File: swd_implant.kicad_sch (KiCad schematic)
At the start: 24 parts, among them J1 U262-161N-4BVC11, J2 G&W pressure contact, J3 50 mil Pin Header, J4 SOICbite, J5 100 mil Pin Header, J6 100 mil Pin header, U1 ATSAMD21E18A, U2 AP2127K-3.3

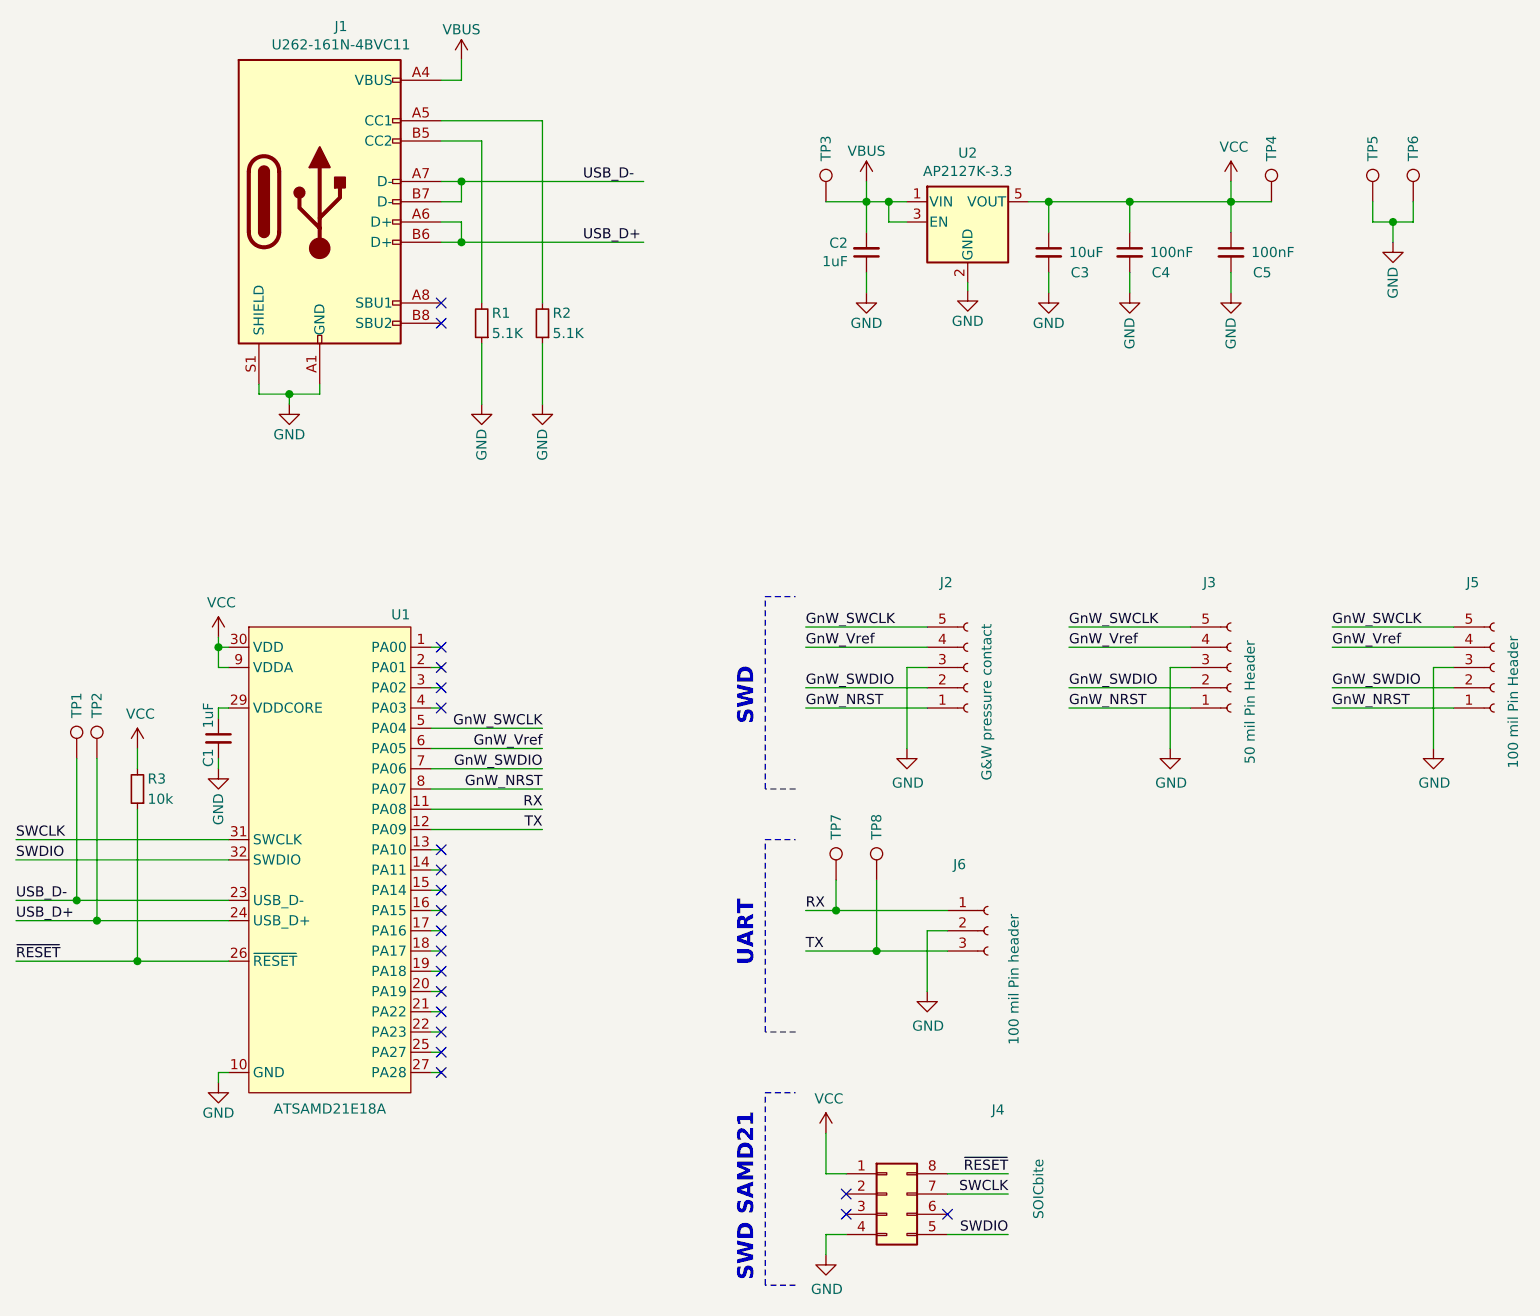
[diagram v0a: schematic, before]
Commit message: New board outline & swd pinout fixes
Changed the board outline to work with castellated edges, making it possible to
solder down instead of just relying on pressure contact.

Also fixed the inverted SWD pinout from upstream.
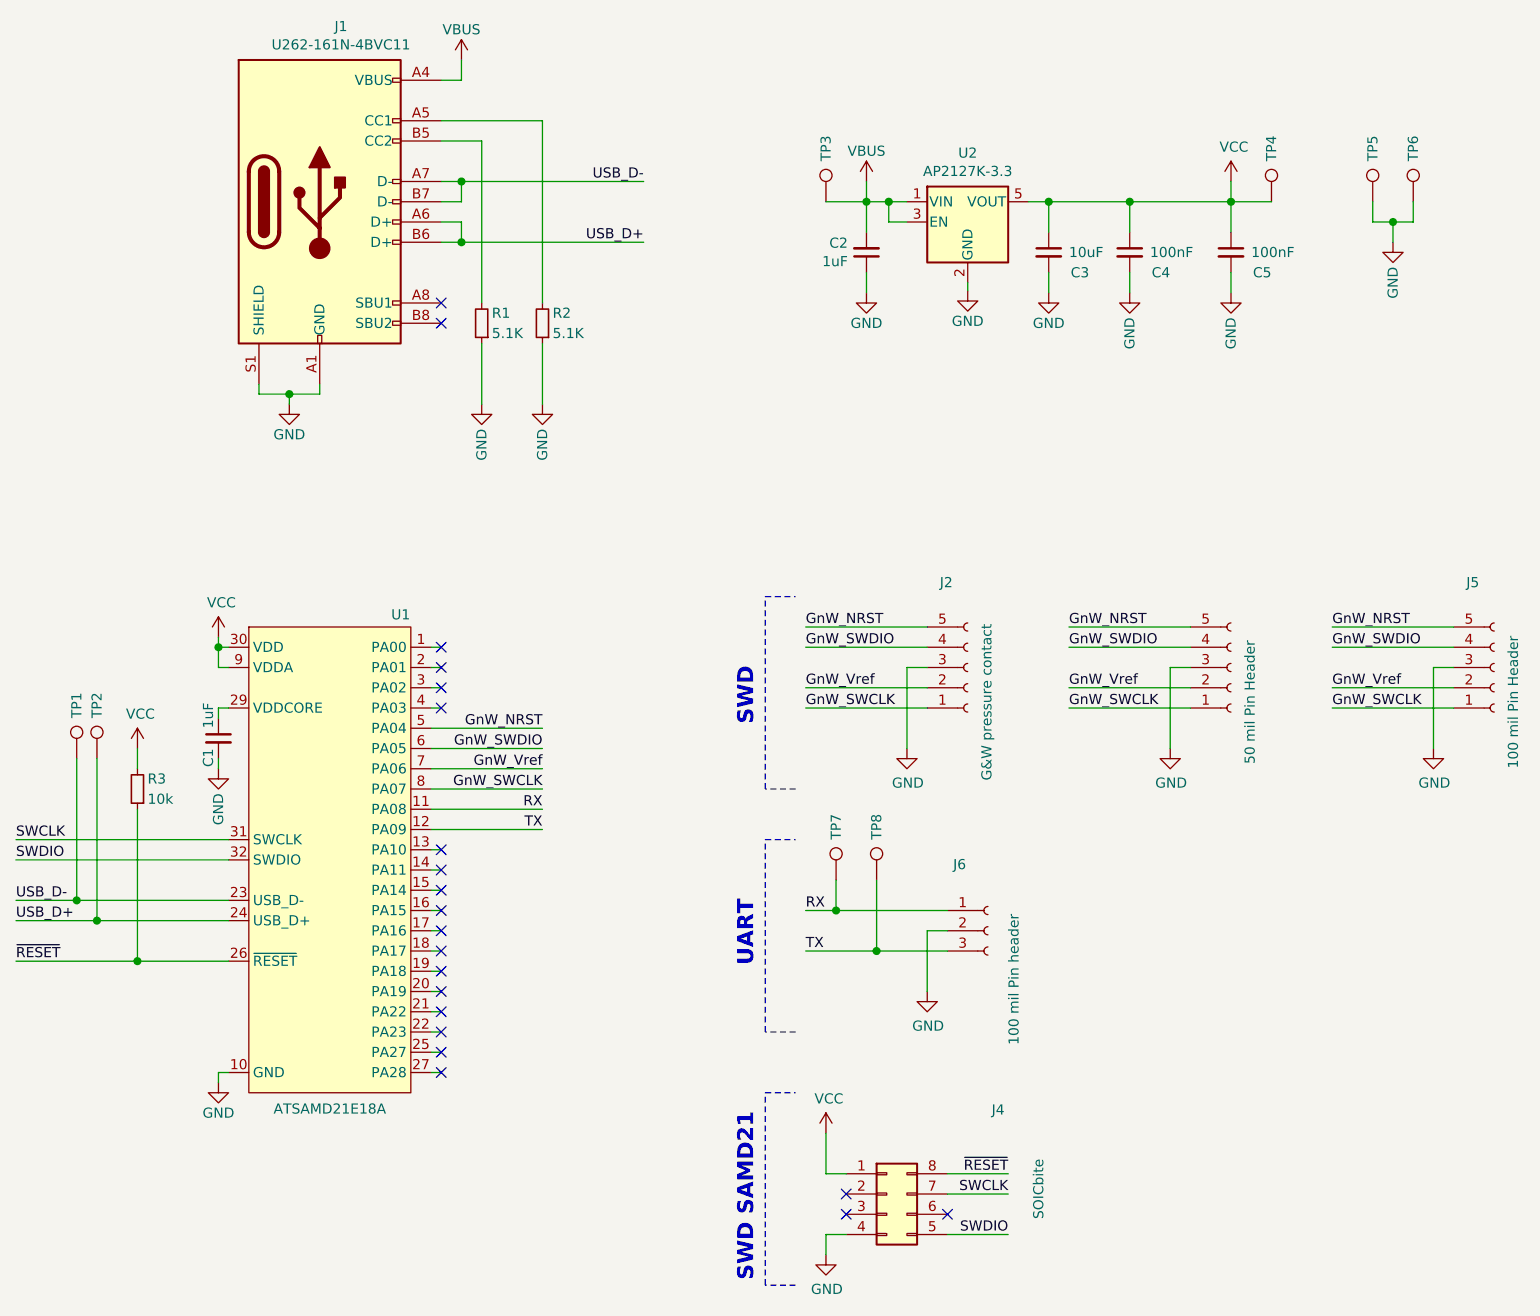
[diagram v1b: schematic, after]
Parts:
- J2: value G&W pressure contact -> G&W pressure contact
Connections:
- net GnW_NRST: now also J2.5 (Pin_5), J3.5 (Pin_5), J5.5 (Pin_5), U1.5 (PA04); no longer J2.1 (Pin_1), J3.1 (Pin_1), J5.1 (Pin_1), U1.8 (PA07)
- net GnW_SWCLK: now also J2.1 (Pin_1), J3.1 (Pin_1), J5.1 (Pin_1), U1.8 (PA07); no longer J2.5 (Pin_5), J3.5 (Pin_5), J5.5 (Pin_5), U1.5 (PA04)
- net GnW_SWDIO: now also J2.4 (Pin_4), J3.4 (Pin_4), J5.4 (Pin_4), U1.6 (PA05); no longer J2.2 (Pin_2), J3.2 (Pin_2), J5.2 (Pin_2), U1.7 (PA06)
- net GnW_Vref: now also J2.2 (Pin_2), J3.2 (Pin_2), J5.2 (Pin_2), U1.7 (PA06); no longer J2.4 (Pin_4), J3.4 (Pin_4), J5.4 (Pin_4), U1.6 (PA05)
- net ~RESET~ renamed ~{RESET}
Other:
- title: (none) -> Game & Watch SWD Implant

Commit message: Prep for fabrication
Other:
- title: Game & Watch SWD Implant -> ${TITLE}
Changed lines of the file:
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@@
 	(paper "A4")
 	(title_block
-		(title "Game & Watch SWD Implant")
-		(rev "Mario")
+		(title "${TITLE}")
+		(rev "${REV}")
+		(comment 1 "${VERSION}")
 	)
 	(text "UART"

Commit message: Add LCSC part numbers
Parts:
- C1, C2: LCSC (none) -> C52923
- C3: LCSC (none) -> C15525
- C4, C5: LCSC (none) -> C1525
- J1: LCSC (none) -> C319148
- R1, R2: LCSC (none) -> C25905
- R3: LCSC (none) -> C25531
- U1: LCSC (none) -> C2052801
- U2: LCSC (none) -> C156285
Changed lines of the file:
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@@
+			)
+		)
+		(property "LCSC" "C1525"
+			(at 190.5 59.69 0)
+			(effects
+				(font
+					(size 1.27 1.27)
+				)
+				(hide yes)
 			)
 		)
@@
 			)
 		)
+		(property "LCSC" "C52923"
+			(at 137.3632 55.9816 0)
+			(effects
+				(font
+					(size 1.27 1.27)
+				)
+				(hide yes)
+			)
+		)
 		(pin "1"
 		)
@@
 			)
 		)
+		(property "LCSC" "C25905"
+			(at 92.71 64.77 0)
+			(effects
+				(font
+					(size 1.27 1.27)
+				)
+				(hide yes)
+			)
+		)
 		(pin "1"
 		)
@@
 			)
 		)
+		(property "LCSC" "C2052801"
+			(at 81.28 102.597 0)
+			(effects
+				(font
+					(size 1.27 1.27)
+				)
+				(hide yes)
+			)
+		)
 		(pin "30"
 		)
@@
 			)
 		)
+		(property "LCSC" "C1525"
+			(at 177.8 59.69 0)
+			(effects
+				(font
+					(size 1.27 1.27)
+				)
+				(hide yes)
+			)
+		)
 		(pin "1"
 		)
@@
 			)
 		)
+		(property "LCSC" "C319148"
+			(at 73.787 28.8098 0)
+			(effects
+				(font
+					(size 1.27 1.27)
+				)
+				(hide yes)
+			)
+		)
 		(pin "S1"
 		)
@@
 		(property "LCSC Part #" "C52923"
 			(at 58.42 118.11 90)
+			(effects
+				(font
+					(size 1.27 1.27)
+				)
+				(hide yes)
+			)
+		)
+		(property "LCSC" "C52923"
+			(at 57.15 119.38 0)
 			(effects
 				(font
@@
 			)
 		)
+		(property "LCSC" "C25905"
+			(at 100.33 64.77 0)
+			(effects
+				(font
+					(size 1.27 1.27)
+				)
+				(hide yes)
+			)
+		)
 		(pin "1"
 		)
@@
 			)
 		)
+		(property "LCSC" "C156285"
+			(at 152.4 44.6848 0)
+			(effects
+				(font
+					(size 1.27 1.27)
+				)
+				(hide yes)
+			)
+		)
 		(pin "1"
 		)
@@
 			)
 		)
+		(property "LCSC" "C15525"
+			(at 167.64 59.69 0)
+			(effects
+				(font
+					(size 1.27 1.27)
+				)
+				(hide yes)
+			)
+		)
 		(pin "1"
 		)
@@
 			(effects
 				(font
+					(size 1.27 1.27)
+				)
+				(hide yes)
+			)
+		)
+		(property "LCSC" "C25531"
+			(at 49.53 123.19 0)
+			(effects
+				(font
